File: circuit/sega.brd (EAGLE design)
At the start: 100.6 x 99 mm, 49 parts, among them P1:C1 100nF, P1:MUX 74LS157N, P1:OK1 PC847, P1:OK2 PC847, P1:R1 10k, P1:R10 750, P1:R11 750, P1:R12 750, P1:R13 750, P1:R14 750, P1:R15 750, P1:R16 750, P1:R17 10k, P1:R2 10k, P1:R3 10k, P1:R4 10k, P1:R5 10k, P1:R6 10k, P1:R7 10k, P1:R8 10k, P1:R9 750, P2:C1 100nF, P2:MUX 74LS157N, P2:OK1 PC847, P2:OK2 PC847, P2:R1 10k, P2:R10 750, P2:R11 750, P2:R12 750, P2:R13 750, P2:R14 750, P2:R15 750, P2:R16 750, P2:R17 10k, P2:R2 10k, P2:R3 10k, P2:R4 10k, P2:R5 10k, P2:R6 10k, P2:R7 10k, P2:R8 10k, P2:R9 750

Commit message: Fix Sega DB9 placement
These connectors were too far from the edge of the board, and it made
it very difficult to connect the extension cord.  I had to modify the
cord to get v1.2 working.  This fixes the placement and updates the
version number to v1.3.
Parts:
- moved P1:X 2.54 mm to (25.4, 8.89)
- moved P2:X 2.54 mm to (74.9, 8.89)
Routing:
- net P2:G|L: track 16.8 -> 19.4 mm
- net P2:SEL: track 31.8 -> 34.3 mm
- net P2:A|B: track 22.6 -> 25.1 mm
- net P1:S|C: track 10.8 -> 13.3 mm
- net P1:G|R: track 17.3 -> 19.8 mm
- net P1:D: track 36.6 -> 39.1 mm
- net P1:A|B: track 19.5 -> 21.9 mm
- net P2:D: track 35.1 -> 37.6 mm
- net P2:G|R: track 18.9 -> 21.4 mm
- net P2:S|C: track 11.1 -> 13.6 mm
- net P1:U: track 37.6 -> 40.1 mm
- net P2:U: track 36.1 -> 38.5 mm
- net P2:GND: track 126.6 -> 129.0 mm
- net P1:VCC: track 99.6 -> 102.0 mm
- net P1:GND: track 127.2 -> 129.6 mm
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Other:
- board text added: "RetCon Sega v1.3"
- board text removed: "RetCon Sega v1.2"
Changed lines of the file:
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@@
 <text x="2.54" y="76.2" size="2.1844" layer="25">RetCon
 Sega
-v1.2</text>
+v1.3</text>
 </plain>
 <attributes>
@@
 <element name="P1:C1" library="capacitor-wima" package="C5B2.5" value="100nF" x="39.37" y="24.13" rot="R270"/>
 <element name="P2:C1" library="capacitor-wima" package="C5B2.5" value="100nF" x="85.09" y="24.13" rot="R270"/>
-<element name="P1:X" library="con-subd" package="F09H" value="" x="25.4" y="11.43" rot="R180">
-<attribute name="OC_NEWARK" value="unknown" x="25.4" y="11.43" size="1.778" layer="27" rot="R180" display="off"/>
-<attribute name="OC_FARNELL" value="unknown" x="25.4" y="11.43" size="1.778" layer="27" rot="R180" display="off"/>
-<attribute name="MPN" value="" x="25.4" y="11.43" size="1.778" layer="27" rot="R180" display="off"/>
-<attribute name="MF" value="" x="25.4" y="11.43" size="1.778" layer="27" rot="R180" display="off"/>
+<element name="P1:X" library="con-subd" package="F09H" value="" x="25.4" y="8.89" rot="R180">
+<attribute name="OC_NEWARK" value="unknown" x="25.4" y="8.89" size="1.778" layer="27" rot="R180" display="off"/>
+<attribute name="OC_FARNELL" value="unknown" x="25.4" y="8.89" size="1.778" layer="27" rot="R180" display="off"/>
+<attribute name="MPN" value="" x="25.4" y="8.89" size="1.778" layer="27" rot="R180" display="off"/>
+<attribute name="MF" value="" x="25.4" y="8.89" size="1.778" layer="27" rot="R180" display="off"/>
 </element>
-<element name="P2:X" library="con-subd" package="F09H" value="" x="74.93" y="11.43" rot="R180">
-<attribute name="OC_NEWARK" value="unknown" x="74.93" y="11.43" size="1.778" layer="27" rot="R180" display="off"/>
-<attribute name="OC_FARNELL" value="unknown" x="74.93" y="11.43" size="1.778" layer="27" rot="R180" display="off"/>
-<attribute name="MPN" value="" x="74.93" y="11.43" size="1.778" layer="27" rot="R180" display="off"/>
-<attribute name="MF" value="" x="74.93" y="11.43" size="1.778" layer="27" rot="R180" display="off"/>
+<element name="P2:X" library="con-subd" package="F09H" value="" x="74.93" y="8.89" rot="R180">
+<attribute name="OC_NEWARK" value="unknown" x="74.93" y="8.89" size="1.778" layer="27" rot="R180" display="off"/>
+<attribute name="OC_FARNELL" value="unknown" x="74.93" y="8.89" size="1.778" layer="27" rot="R180" display="off"/>
+<attribute name="MPN" value="" x="74.93" y="8.89" size="1.778" layer="27" rot="R180" display="off"/>
+<attribute name="MF" value="" x="74.93" y="8.89" size="1.778" layer="27" rot="R180" display="off"/>
 </element>
 <element name="PI" library="pizero" package="PIZERO_THOUGH_HOLE" value="PIZERO_THROUGH_HOLE" x="82.55" y="99.06" rot="R180"/>
@@
 <wire x1="27.178" y1="17.018" x2="27.178" y2="13.081" width="0.127" layer="1"/>
 <wire x1="30.48" y1="20.32" x2="27.178" y2="17.018" width="0.127" layer="1"/>
-<wire x1="24.13" y1="10.16" x2="24.0284" y2="10.16" width="0.127" layer="1"/>
+<wire x1="24.13" y1="10.16" x2="24.0284" y2="7.62" width="0.127" layer="1"/>
 <wire x1="25.4" y1="45.72" x2="24.13" y2="45.72" width="0.127" layer="1"/>
 <wire x1="26.289" y1="46.609" x2="25.4" y2="45.72" width="0.127" layer="1"/>
@@
 <wire x1="73.66" y1="17.78" x2="73.66" y2="10.16" width="0.127" layer="1"/>
 <wire x1="76.2" y1="20.32" x2="73.66" y2="17.78" width="0.127" layer="1"/>
-<wire x1="73.66" y1="10.16" x2="73.5584" y2="10.16" width="0.127" layer="1"/>
+<wire x1="73.66" y1="10.16" x2="73.5584" y2="7.62" width="0.127" layer="1"/>
 <wire x1="71.12" y1="45.72" x2="69.85" y2="45.72" width="0.127" layer="1"/>
 <wire x1="72.009" y1="46.609" x2="71.12" y2="45.72" width="0.127" layer="1"/>
@@
 <wire x1="19.431" y1="25.908" x2="19.431" y2="19.304" width="0.127" layer="1"/>
 <wire x1="19.939" y1="26.416" x2="19.431" y2="25.908" width="0.127" layer="1"/>
-<wire x1="19.812" y1="12.7" x2="19.9136" y2="12.7" width="0.127" layer="1"/>
+<wire x1="19.812" y1="12.7" x2="19.9136" y2="10.16" width="0.127" layer="1"/>
 <wire x1="13.97" y1="23.495" x2="13.97" y2="31.75" width="0.127" layer="1"/>
 <wire x1="16.891" y1="20.574" x2="13.97" y2="23.495" width="0.127" layer="1"/>
@@
 <wire x1="83.82" y1="20.32" x2="78.74" y2="20.32" width="0.127" layer="1"/>
 <wire x1="85.09" y1="21.59" x2="83.82" y2="20.32" width="0.127" layer="1"/>
-<wire x1="70.739" y1="12.7" x2="69.4436" y2="12.7" width="0.127" layer="16"/>
+<wire x1="70.739" y1="12.7" x2="69.4436" y2="10.16" width="0.127" layer="16"/>
 <wire x1="71.755" y1="11.684" x2="70.739" y2="12.7" width="0.127" layer="16"/>
 <wire x1="78.105" y1="11.684" x2="71.755" y2="11.684" width="0.127" layer="16"/>
@@
 <wire x1="38.1" y1="40.64" x2="38.1" y2="23.495" width="0.127" layer="16"/>
 <wire x1="39.37" y1="41.91" x2="38.1" y2="40.64" width="0.127" layer="16"/>
-<wire x1="30.988" y1="12.7" x2="30.8864" y2="12.7" width="0.127" layer="16"/>
+<wire x1="30.988" y1="12.7" x2="30.8864" y2="10.16" width="0.127" layer="16"/>
 </signal>
 <signal name="P2:U">
@@
 <wire x1="83.947" y1="40.767" x2="83.947" y2="34.417" width="0.127" layer="16"/>
 <wire x1="85.09" y1="41.91" x2="83.947" y2="40.767" width="0.127" layer="16"/>
-<wire x1="80.518" y1="12.7" x2="80.4164" y2="12.7" width="0.127" layer="16"/>
+<wire x1="80.518" y1="12.7" x2="80.4164" y2="10.16" width="0.127" layer="16"/>
 </signal>
 <signal name="P1:A">
@@
 <wire x1="32.131" y1="39.751" x2="32.131" y2="20.066" width="0.127" layer="16"/>
 <wire x1="34.29" y1="41.91" x2="32.131" y2="39.751" width="0.127" layer="16"/>
-<wire x1="28.194" y1="12.7" x2="28.1432" y2="12.7" width="0.127" layer="16"/>
+<wire x1="28.194" y1="12.7" x2="28.1432" y2="10.16" width="0.127" layer="16"/>
 </signal>
 <signal name="P2:D">
@@
 <wire x1="77.724" y1="39.624" x2="77.724" y2="12.7" width="0.127" layer="16"/>
 <wire x1="80.01" y1="41.91" x2="77.724" y2="39.624" width="0.127" layer="16"/>
-<wire x1="77.724" y1="12.7" x2="77.6732" y2="12.7" width="0.127" layer="16"/>
+<wire x1="77.724" y1="12.7" x2="77.6732" y2="10.16" width="0.127" layer="16"/>
 </signal>
 <signal name="P1:B">
@@
 <wire x1="24.511" y1="21.336" x2="25.4" y2="22.225" width="0.127" layer="1"/>
 <wire x1="24.511" y1="13.589" x2="24.511" y2="21.336" width="0.127" layer="1"/>
-<wire x1="25.4" y1="12.7" x2="24.511" y2="13.589" width="0.127" layer="1"/>
+<wire x1="25.4" y1="10.16" x2="24.511" y2="13.589" width="0.127" layer="1"/>
 </signal>
 <signal name="P2:G|L">
@@
 <wire x1="71.12" y1="24.765" x2="71.12" y2="27.94" width="0.127" layer="16"/>
 <wire x1="74.93" y1="20.955" x2="71.12" y2="24.765" width="0.127" layer="16"/>
-<wire x1="74.93" y1="12.7" x2="74.93" y2="20.955" width="0.127" layer="16"/>
+<wire x1="74.93" y1="10.16" x2="74.93" y2="20.955" width="0.127" layer="16"/>
 </signal>
 <signal name="P1:G|R">
@@
 <wire x1="18.923" y1="16.383" x2="18.923" y2="21.082" width="0.127" layer="16"/>
 <wire x1="22.606" y1="12.7" x2="18.923" y2="16.383" width="0.127" layer="16"/>
-<wire x1="22.606" y1="12.7" x2="22.6568" y2="12.7" width="0.127" layer="16"/>
+<wire x1="22.606" y1="12.7" x2="22.6568" y2="10.16" width="0.127" layer="16"/>
 </signal>
 <signal name="P2:G|R">
@@
 <wire x1="67.691" y1="17.145" x2="67.691" y2="20.574" width="0.127" layer="16"/>
 <wire x1="72.136" y1="12.7" x2="67.691" y2="17.145" width="0.127" layer="16"/>
-<wire x1="72.136" y1="12.7" x2="72.1868" y2="12.7" width="0.127" layer="16"/>
+<wire x1="72.136" y1="12.7" x2="72.1868" y2="10.16" width="0.127" layer="16"/>
 </signal>
 <signal name="P1:A|B">
@@
 <wire x1="28.448" y1="11.176" x2="22.733" y2="11.176" width="0.127" layer="16"/>
 <wire x1="29.464" y1="10.16" x2="28.448" y2="11.176" width="0.127" layer="16"/>
-<wire x1="29.464" y1="10.16" x2="29.5148" y2="10.16" width="0.127" layer="16"/>
+<wire x1="29.464" y1="10.16" x2="29.5148" y2="7.62" width="0.127" layer="16"/>
 </signal>
 <signal name="P2:A|B">
@@
 <wire x1="77.978" y1="11.176" x2="69.596" y2="11.176" width="0.127" layer="16"/>
 <wire x1="78.994" y1="10.16" x2="77.978" y2="11.176" width="0.127" layer="16"/>
-<wire x1="78.994" y1="10.16" x2="79.0448" y2="10.16" width="0.127" layer="16"/>
+<wire x1="78.994" y1="10.16" x2="79.0448" y2="7.62" width="0.127" layer="16"/>
 </signal>
 <signal name="P1:SEL">
@@
 <wire x1="40.64" y1="27.94" x2="33.02" y2="27.94" width="0.127" layer="1"/>
 <wire x1="44.45" y1="31.75" x2="40.64" y2="27.94" width="0.127" layer="1"/>
-<wire x1="27.051" y1="10.16" x2="26.7716" y2="10.16" width="0.127" layer="1"/>
+<wire x1="27.051" y1="10.16" x2="26.7716" y2="7.62" width="0.127" layer="1"/>
 <wire x1="29.845" y1="12.954" x2="27.051" y2="10.16" width="0.127" layer="1"/>
 <wire x1="29.845" y1="17.78" x2="29.845" y2="12.954" width="0.127" layer="1"/>
@@
 <wire x1="77.851" y1="27.051" x2="77.851" y2="20.066" width="0.127" layer="1"/>
 <wire x1="78.74" y1="27.94" x2="77.851" y2="27.051" width="0.127" layer="1"/>
-<wire x1="76.327" y1="10.16" x2="76.3016" y2="10.16" width="0.127" layer="1"/>
+<wire x1="76.327" y1="10.16" x2="76.3016" y2="7.62" width="0.127" layer="1"/>
 </signal>
 <signal name="P1:N$2">
@@
 <wire x1="21.336" y1="12.827" x2="22.86" y2="14.351" width="0.127" layer="1"/>
 <wire x1="21.336" y1="10.16" x2="21.336" y2="12.827" width="0.127" layer="1"/>
-<wire x1="21.336" y1="10.16" x2="21.2852" y2="10.16" width="0.127" layer="1"/>
+<wire x1="21.336" y1="10.16" x2="21.2852" y2="7.62" width="0.127" layer="1"/>
 </signal>
 <signal name="P2:S|C">
@@
 <wire x1="70.739" y1="12.827" x2="68.58" y2="14.986" width="0.127" layer="1"/>
 <wire x1="70.739" y1="10.16" x2="70.739" y2="12.827" width="0.127" layer="1"/>
-<wire x1="70.739" y1="10.16" x2="70.8152" y2="10.16" width="0.127" layer="1"/>
+<wire x1="70.739" y1="10.16" x2="70.8152" y2="7.62" width="0.127" layer="1"/>
 </signal>
 </signals>

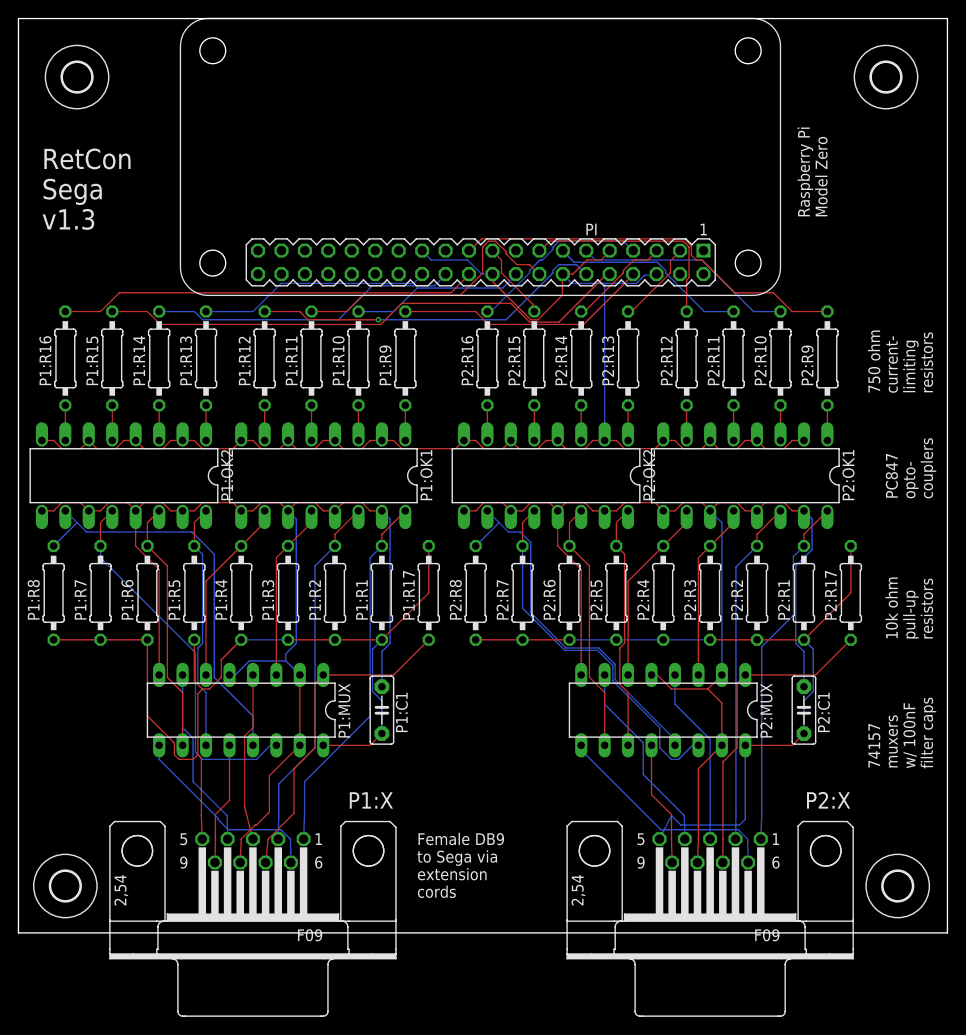
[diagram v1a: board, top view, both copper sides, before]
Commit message: Replace optocouplers with transistors
This makes the board cheaper and frees up some space for additional
hardware in future revisions.  This is hardware v1.4.
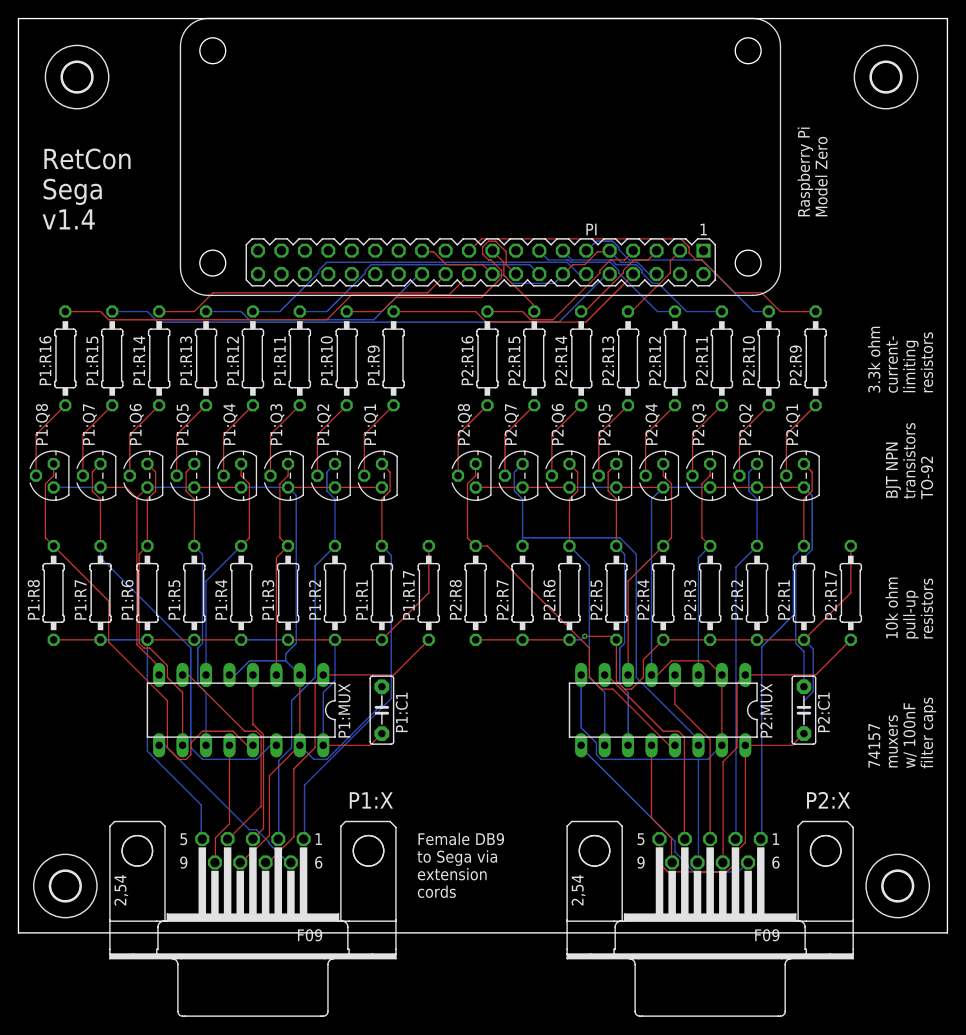
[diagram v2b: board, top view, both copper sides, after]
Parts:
- removed P1:OK1, P1:OK2, P2:OK1, P2:OK2: PC847, optocoupler:DIL16
- added P1:Q1, P1:Q2, P1:Q3, P1:Q4, P1:Q5, P1:Q6, P1:Q7, P1:Q8, P2:Q1, P2:Q2, P2:Q3, P2:Q4, P2:Q5, P2:Q6, P2:Q7, P2:Q8: 2N3904, transistor-npn:TO92
- P1:R10, P1:R11, P1:R12, P1:R13, P1:R14, P1:R15, P1:R16, P1:R9, P2:R10, P2:R11, P2:R12, P2:R13, P2:R14, P2:R15, P2:R16, P2:R9: value 750 -> 3.3k
- moved P1:R12 1.27 mm to (25.4, 62.2)
- moved P1:R11 1.27 mm to (30.5, 62.2)
- moved P1:R10 1.27 mm to (35.6, 62.2)
- moved P1:R9 1.27 mm to (40.6, 62.2)
- moved P2:R10 1.27 mm to (81.3, 62.2)
- moved P2:R11 1.27 mm to (76.2, 62.2)
- moved P2:R12 1.27 mm to (71.1, 62.2)
- moved P2:R9 1.27 mm to (86.4, 62.2)
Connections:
- net N$2: no longer P1:OK1.2, P1:OK1.4, P1:OK1.6, P1:OK1.8, P1:OK2.2, P1:OK2.4, P1:OK2.6, P1:OK2.8, P2:OK1.2, P2:OK1.4, P2:OK1.6, P2:OK1.8, P2:OK2.2, P2:OK2.4, P2:OK2.6, P2:OK2.8
- net P1:A: now also P1:Q5.1; no longer P1:OK2.16
- net P1:B: now also P1:Q6.1; no longer P1:OK2.14
- net P1:C: now also P1:Q8.1; no longer P1:OK2.10
- net P1:D: now also P1:Q2.1; no longer P1:OK1.14
- net P1:GND: now also P1:Q1.3, P1:Q2.3, P1:Q3.3, P1:Q4.3, P1:Q5.3, P1:Q6.3, P1:Q7.3, P1:Q8.3; no longer P1:OK1.11, P1:OK1.13, P1:OK1.15, P1:OK1.9, P1:OK2.11, P1:OK2.13, P1:OK2.15, P1:OK2.9
- net P1:L: now also P1:Q3.1; no longer P1:OK1.12
- net P1:N$10: now also P1:Q3.2; no longer P1:OK1.5
- net P1:N$11: now also P1:Q4.2; no longer P1:OK1.7
- net P1:N$12: now also P1:Q5.2; no longer P1:OK2.1
- net P1:N$13: now also P1:Q6.2; no longer P1:OK2.3
- net P1:N$14: now also P1:Q7.2; no longer P1:OK2.5
- net P1:N$15: now also P1:Q8.2; no longer P1:OK2.7
- net P1:N$2: now also P1:Q1.2; no longer P1:OK1.1
- net P1:N$9: now also P1:Q2.2; no longer P1:OK1.3
- net P1:R: now also P1:Q4.1; no longer P1:OK1.10
- net P1:S: now also P1:Q7.1; no longer P1:OK2.12
- net P1:U: now also P1:Q1.1; no longer P1:OK1.16
- net P2:A: now also P2:Q5.1; no longer P2:OK2.16
- net P2:B: now also P2:Q6.1; no longer P2:OK2.14
- net P2:C: now also P2:Q8.1; no longer P2:OK2.10
- net P2:D: now also P2:Q2.1; no longer P2:OK1.14
- net P2:GND: now also P2:Q1.3, P2:Q2.3, P2:Q3.3, P2:Q4.3, P2:Q5.3, P2:Q6.3, P2:Q7.3, P2:Q8.3; no longer P2:OK1.11, P2:OK1.13, P2:OK1.15, P2:OK1.9, P2:OK2.11, P2:OK2.13, P2:OK2.15, P2:OK2.9
- net P2:L: now also P2:Q3.1; no longer P2:OK1.12
- net P2:N$10: now also P2:Q3.2; no longer P2:OK1.5
- net P2:N$11: now also P2:Q4.2; no longer P2:OK1.7
- net P2:N$12: now also P2:Q5.2; no longer P2:OK2.1
- net P2:N$13: now also P2:Q6.2; no longer P2:OK2.3
- net P2:N$14: now also P2:Q7.2; no longer P2:OK2.5
- net P2:N$15: now also P2:Q8.2; no longer P2:OK2.7
- net P2:N$2: now also P2:Q1.2; no longer P2:OK1.1
- net P2:N$9: now also P2:Q2.2; no longer P2:OK1.3
- net P2:R: now also P2:Q4.1; no longer P2:OK1.10
- net P2:S: now also P2:Q7.1; no longer P2:OK2.12
- net P2:U: now also P2:Q1.1; no longer P2:OK1.16
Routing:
- net N$2: track 150.0 -> 29.5 mm
- net P2:VCC: track 85.2 -> 99.0 mm, vias 0 -> 1
- net P1:VCC: track 102.0 -> 90.8 mm
- net N$14: track 18.8 -> 28.7 mm
- net P1:GND: track 129.6 -> 122.2 mm
- net P2:S: track 39.8 -> 46.2 mm
- net N$7: track 24.0 -> 17.6 mm
- net P1:B: track 27.5 -> 33.9 mm
- net P1:U: track 40.1 -> 45.8 mm
- net P2:B: track 27.5 -> 32.8 mm
- net P1:S: track 40.7 -> 45.9 mm
- net P1:A: track 26.9 -> 32.2 mm
- net P2:A: track 26.9 -> 32.2 mm
- net P2:N$11: track 3.81 -> 8.94 mm
- net P2:N$14: track 3.81 -> 8.94 mm
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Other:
- board text added: "3.3k ohm current- limiting resistors"
- board text added: "BJT NPN transistors TO-92"
- board text added: "RetCon Sega v1.4"
- board text removed: "750 ohm current- limiting resistors"
- board text removed: "PC847 opto- couplers"
- board text removed: "RetCon Sega v1.3"

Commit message: Fix Sega board, v1.5
 - Fix pin names and directions
 - Fix missing connections to GND
 - Add missing junctions to the schematic

Closes #19
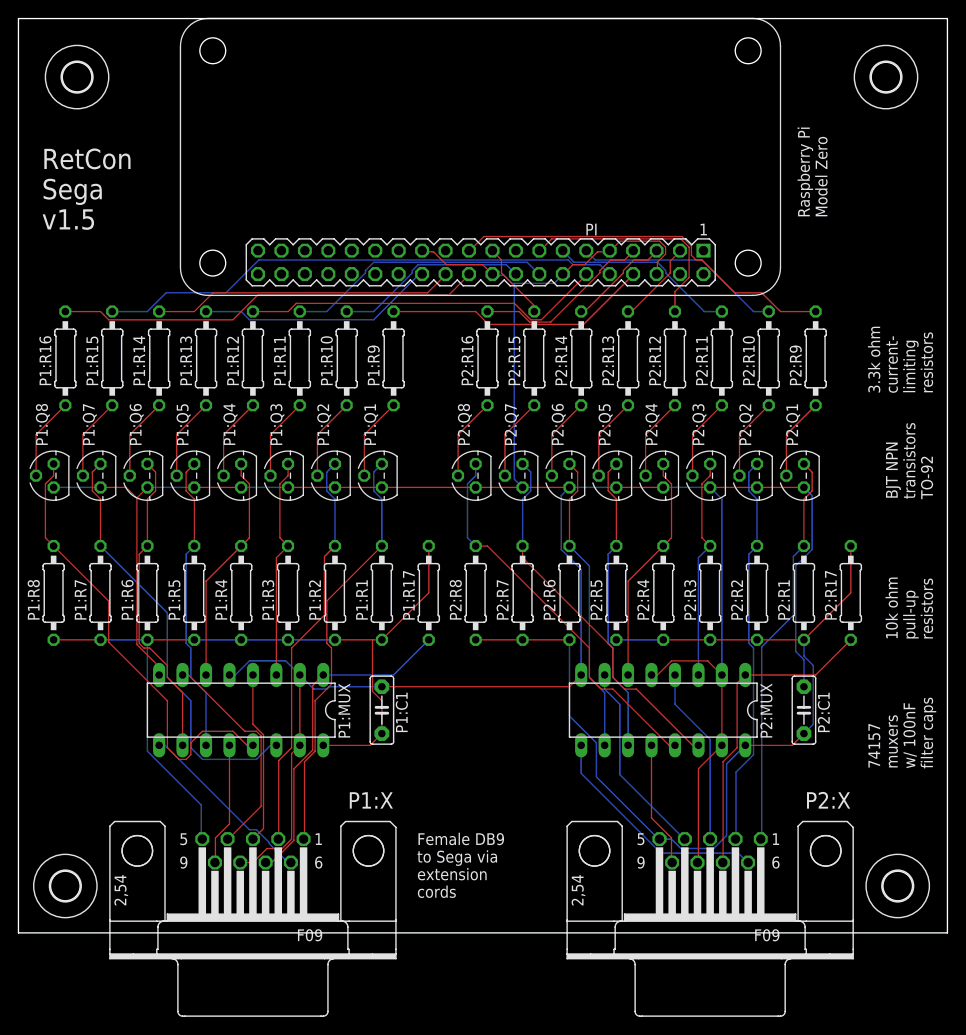
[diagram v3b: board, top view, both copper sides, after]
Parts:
- P1:X, P2:X: value (none) -> -
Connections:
- removed net N$2: PI.14, PI.20, PI.25, PI.6, PI.9
- removed net P1:GND: P1:C1.1, P1:MUX.15, P1:MUX.2, P1:MUX.5, P1:MUX.8, P1:Q1.3, P1:Q2.3, P1:Q3.3, P1:Q4.3, P1:Q5.3, P1:Q6.3, P1:Q7.3, P1:Q8.3, P1:X.8
- removed net P2:GND: P2:C1.1, P2:MUX.15, P2:MUX.2, P2:MUX.5, P2:MUX.8, P2:Q1.3, P2:Q2.3, P2:Q3.3, P2:Q4.3, P2:Q5.3, P2:Q6.3, P2:Q7.3, P2:Q8.3, P2:X.8
- new net GND: P1:C1.1, P1:MUX.15, P1:MUX.2, P1:MUX.5, P1:MUX.8, P1:Q1.3, P1:Q2.3, P1:Q3.3, P1:Q4.3, P1:Q5.3, P1:Q6.3, P1:Q7.3, P1:Q8.3, P1:X.8, P2:C1.1, P2:MUX.15, P2:MUX.2, P2:MUX.5, P2:MUX.8, P2:Q1.3, P2:Q2.3, P2:Q3.3, P2:Q4.3, P2:Q5.3, P2:Q6.3, P2:Q7.3, P2:Q8.3, P2:X.8, PI.14, PI.20, PI.25, PI.6, PI.9
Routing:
- net GND: track 0.00 -> 319.6 mm
- net P2:GND: track 131.0 -> 0.00 mm
- net P1:GND: track 122.2 -> 0.00 mm
- net N$2: track 29.5 -> 0.00 mm
- net N$14: track 28.7 -> 21.0 mm
- net N$7: track 17.6 -> 24.7 mm
- net P2:VCC: track 99.0 -> 105.2 mm, vias 1 -> 0
- net P2:S: track 46.2 -> 40.2 mm
- net P1:VCC: track 90.8 -> 89.4 mm
- net P2:G|R: track 22.5 -> 21.4 mm
- net N$1: track 23.5 -> 22.5 mm
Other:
- board text added: "RetCon Sega v1.5"
- board text removed: "RetCon Sega v1.4"
